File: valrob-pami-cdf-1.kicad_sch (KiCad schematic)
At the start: 115 parts, among them J1 Conn_01x04, J10 Conn_01x04_Pin, J3 USB_C_Receptacle_USB2.0_14P, J4 Conn_01x02, M1 Motor_Servo, Q1 Q_NMOS, Q2 Q_NMOS, Q3 Q_NMOS, SW1 SW_SPST, SW2 SW_Push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

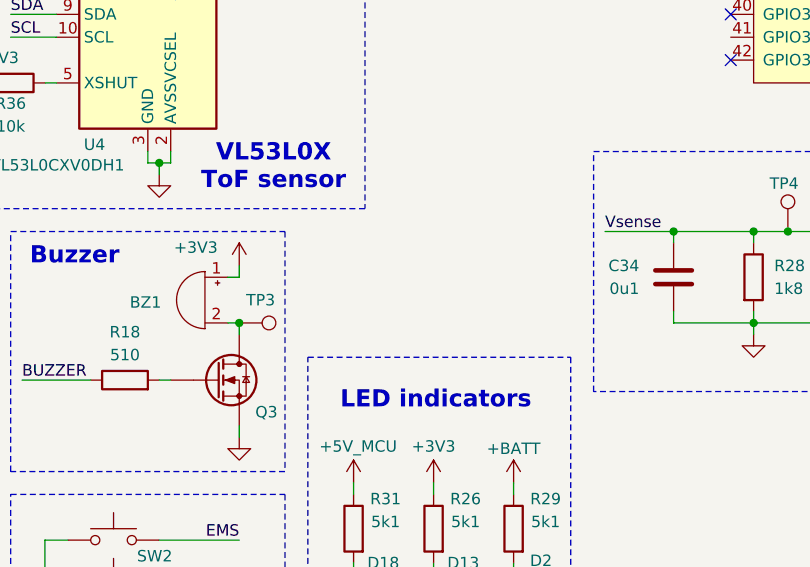
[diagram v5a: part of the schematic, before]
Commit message: schem: add mounting holes
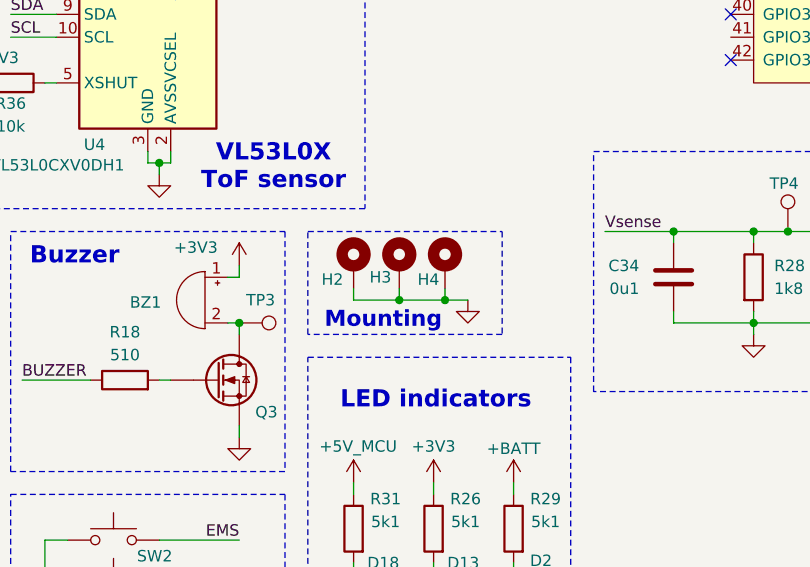
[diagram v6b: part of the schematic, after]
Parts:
- added H2, H3, H4: MountingHole_Pad, MountingHole:MountingHole_2.2mm_M2_Pad_Via, symbol Mechanical:MountingHole_Pad
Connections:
- net GND: now also H2.1, H3.1, H4.1
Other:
- note added: "Mounting"

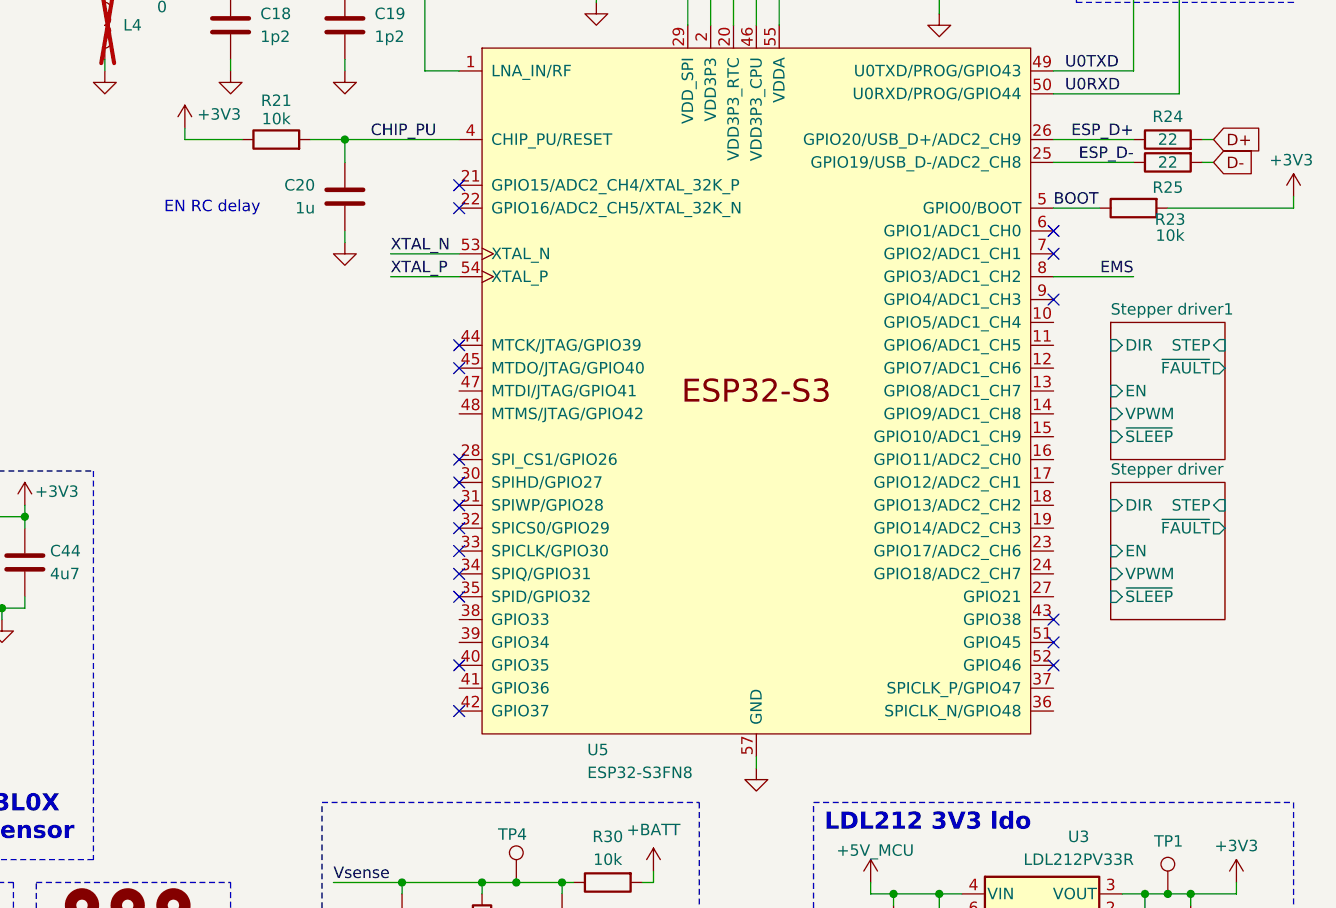
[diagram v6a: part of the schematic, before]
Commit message: schem: connecto all gpios to mcu
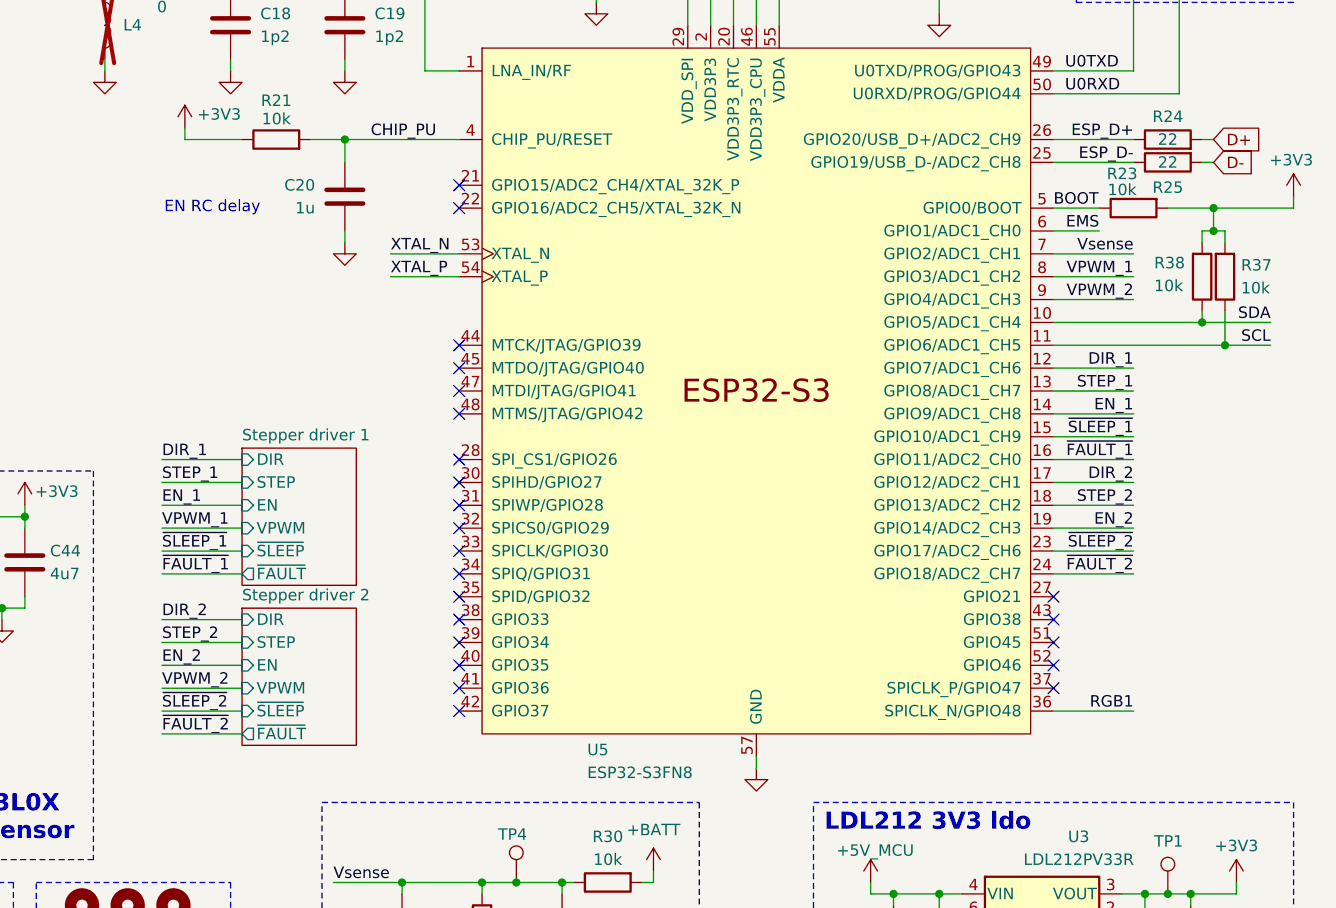
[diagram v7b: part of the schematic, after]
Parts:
- added R37, R38: 10k, Resistor_SMD:R_0402_1005Metric, symbol Device:R
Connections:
- net +3V3: now also R37.2, R38.2
- net EMS: now also U5.6 (GPIO1/ADC1_CH0); no longer U5.8 (GPIO3/ADC1_CH2)
- net RGB1: now also U5.36 (SPICLK_N/GPIO48)
- net SCL: now also U5.11 (GPIO6/ADC1_CH5), R37.1
- net SDA: now also U5.10 (GPIO5/ADC1_CH4), R38.1
- net Vsense: now also U5.7 (GPIO2/ADC1_CH1)
- net DIR_1: now reaches U5.12 (GPIO7/ADC1_CH6)
- net STEP_1: now reaches U5.13 (GPIO8/ADC1_CH7)
- net EN_1: now reaches U5.14 (GPIO9/ADC1_CH8)
- net ~{SLEEP_1}: now reaches U5.15 (GPIO10/ADC1_CH9)
- net ~{FAULT_1}: now reaches U5.16 (GPIO11/ADC2_CH0)
- net DIR_2: now reaches U5.17 (GPIO12/ADC2_CH1)
- net STEP_2: now reaches U5.18 (GPIO13/ADC2_CH2)
- net EN_2: now reaches U5.19 (GPIO14/ADC2_CH3)
- net ~{SLEEP_2}: now reaches U5.23 (GPIO17/ADC2_CH6)
- net ~{FAULT_2}: now reaches U5.24 (GPIO18/ADC2_CH7)
- net VPWM_2: now reaches U5.9 (GPIO4/ADC1_CH3)
- new net VPWM_1: U5.8 (GPIO3/ADC1_CH2)
- no-connect marks 22 -> 26
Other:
- sheet Stepper driver renamed Stepper driver 1
- removed sheet Stepper driver1
- added sheet Stepper driver 2 (stepper.kicad_sch)

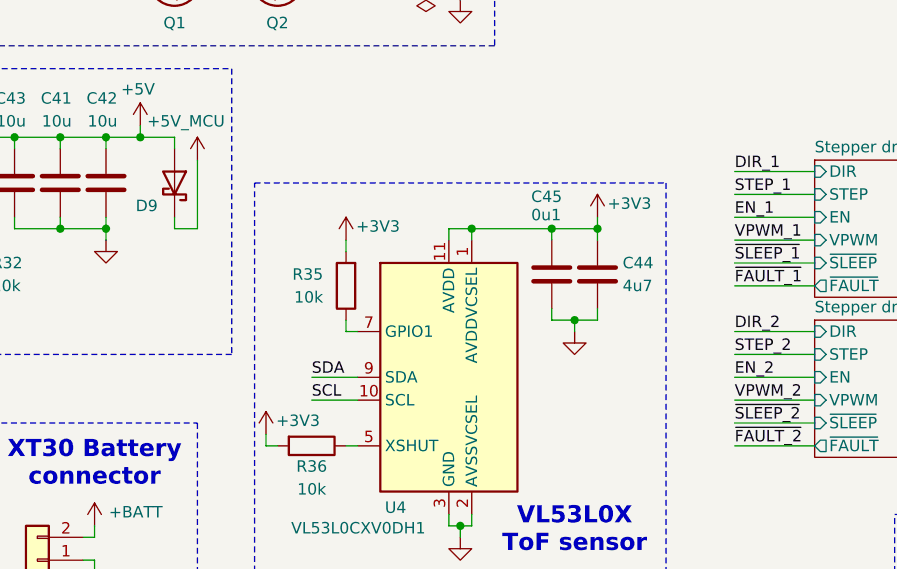
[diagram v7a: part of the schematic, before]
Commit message: schem: add test points
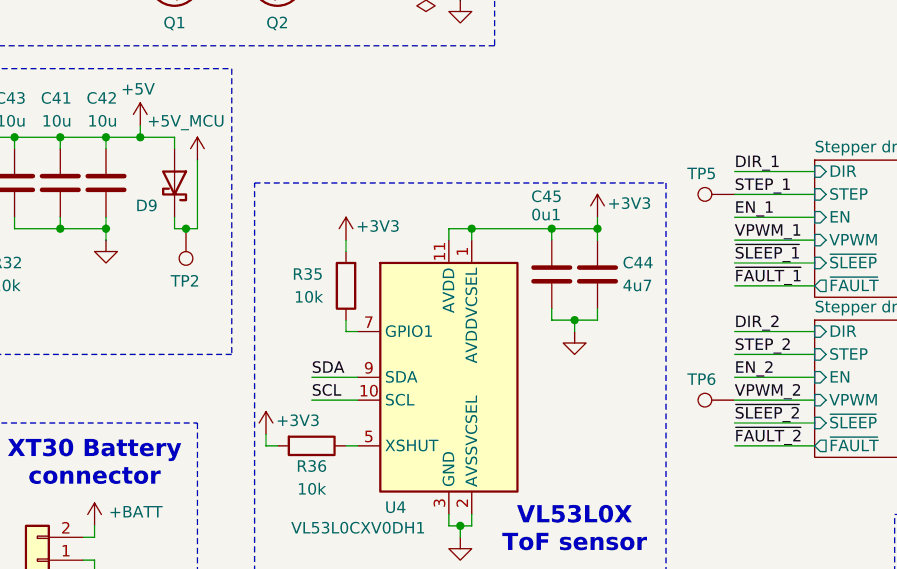
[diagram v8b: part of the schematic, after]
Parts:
- added TP2, TP5, TP6: TestPoint, TestPoint:TestPoint_Pad_D2.0mm, symbol Connector:TestPoint
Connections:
- net +5V_MCU: now also TP2.1
- net STEP_1: now also TP5.1
- net VPWM_2: now also TP6.1
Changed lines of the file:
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@@
 	)
 	(junction
+		(at 95.25 105.41)
+		(diameter 0)
+		(color 0 0 0 0)
+	)
+	(junction
 		(at 90.17 59.69)
 		(diameter 0)
@@
 	(wire
 		(pts
-			(xy 93.98 105.41) (xy 96.52 105.41)
+			(xy 93.98 105.41) (xy 95.25 105.41)
 		)
 		(stroke
@@
 	(wire
 		(pts
+			(xy 95.25 105.41) (xy 96.52 105.41)
+		)
+		(stroke
+			(width 0)
+			(type default)
+		)
+	)
+	(wire
+		(pts
 			(xy 50.8 78.74) (xy 52.07 78.74)
 		)
@@
 	)
 	(symbol
+		(lib_id "Connector:TestPoint")
+		(at 156.21 101.6 90)
+		(unit 1)
+		(exclude_from_sim no)
+		(in_bom no)
+		(on_board yes)
+		(dnp no)
+		(property "Reference" "TP5"
+			(at 154.178 99.314 90)
+			(effects
+				(font
+					(size 1.27 1.27)
+				)
+				(justify left)
+			)
+		)
+		(property "Value" "TestPoint"
+			(at 154.1779 99.06 0)
+			(effects
+				(font
+					(size 1.27 1.27)
+				)
+				(justify left)
+				(hide yes)
+			)
+		)
+		(property "Footprint" "TestPoint:TestPoint_Pad_D2.0mm"
+			(at 156.21 96.52 0)
+			(effects
+				(font
+					(size 1.27 1.27)
+				)
+				(hide yes)
+			)
+		)
+		(property "Datasheet" "~"
+			(at 156.21 96.52 0)
+			(effects
+				(font
+					(size 1.27 1.27)
+				)
+				(hide yes)
+			)
+		)
+		(property "Description" "test point"
+			(at 156.21 101.6 0)
+			(effects
+				(font
+					(size 1.27 1.27)
+				)
+				(hide yes)
+			)
+		)
+		(pin "1"
+		)
+		(instances
+			(project "valrob-pami-cdf-1"
+				(path "/453def7e-2a78-4c3c-a4b7-f12883e5bdd2"
+					(reference "TP5")
+					(unit 1)
+				)
+			)
+		)
+	)
+	(symbol
 		(lib_id "power:+3V3")
 		(at 134.62 149.86 0)
@@
 	)
 	(symbol
+		(lib_id "Connector:TestPoint")
+		(at 95.25 105.41 180)
+		(unit 1)
+		(exclude_from_sim no)
+		(in_bom no)
+		(on_board yes)
+		(dnp no)
+		(property "Reference" "TP2"
+			(at 96.774 111.252 0)
+			(effects
+				(font
+					(size 1.27 1.27)
+				)
+				(justify left)
+			)
+		)
+		(property "Value" "TestPoint"
+			(at 92.71 107.4421 0)
+			(effects
+				(font
+					(size 1.27 1.27)
+				)
+				(justify left)
+				(hide yes)
+			)
+		)
+		(property "Footprint" "TestPoint:TestPoint_Pad_D2.0mm"
+			(at 90.17 105.41 0)
+			(effects
+				(font
+					(size 1.27 1.27)
+				)
+				(hide yes)
+			)
+		)
+		(property "Datasheet" "~"
+			(at 90.17 105.41 0)
+			(effects
+				(font
+					(size 1.27 1.27)
+				)
+				(hide yes)
+			)
+		)
+		(property "Description" "test point"
+			(at 95.25 105.41 0)
+			(effects
+				(font
+					(size 1.27 1.27)
+				)
+				(hide yes)
+			)
+		)
+		(pin "1"
+		)
+		(instances
+			(project "valrob-pami-cdf-1"
+				(path "/453def7e-2a78-4c3c-a4b7-f12883e5bdd2"
+					(reference "TP2")
+					(unit 1)
+				)
+			)
+		)
+	)
+	(symbol
 		(lib_id "Device:R")
 		(at 44.45 166.37 270)
@@
 					(unit 1)
 				)
+			)
+		)
+	)
+	(symbol
+		(lib_id "Connector:TestPoint")
+		(at 156.21 124.46 90)
+		(unit 1)
+		(exclude_from_sim no)
+		(in_bom no)
+		(on_board yes)
+		(dnp no)
+		(property "Reference" "TP6"
+			(at 154.178 122.174 90)
+			(effects
+				(font
+					(size 1.27 1.27)
+				)
+				(justify left)
+			)
+		)
+		(property "Value" "TestPoint"
+			(at 154.1779 121.92 0)
+			(effects
+				(font
+					(size 1.27 1.27)
+				)
+				(justify left)
+				(hide yes)
+			)
+		)
+		(property "Footprint" "TestPoint:TestPoint_Pad_D2.0mm"
+			(at 156.21 119.38 0)
+			(effects
+				(font
+					(size 1.27 1.27)
+				)
+				(hide yes)
+			)
+		)
+		(property "Datasheet" "~"
+			(at 156.21 119.38 0)
+			(effects
+				(font
+					(size 1.27 1.27)
+				)
+				(hide yes)
+			)
+		)
+		(property "Description" "test point"
+			(at 156.21 124.46 0)
+			(effects
+				(font
+					(size 1.27 1.27)
+				)
+				(hide yes)
+			)
+		)
+		(pin "1"
+		)
+		(instances
+			(project "valrob-pami-cdf-1"
+				(path "/453def7e-2a78-4c3c-a4b7-f12883e5bdd2"
+					(reference "TP6")
+					(unit 1)
+				)
